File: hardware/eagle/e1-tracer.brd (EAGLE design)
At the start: 100 x 75 mm, 120 parts, among them IC1 MCP1703T-1202E/CB, IC2 W25Q80DVSNIG, IC3 TLV70233DBVR, IC4 ASEM1-12.000MHZ-LC-T, J1 PASSTHROUGH, M1 MENTOR_12701001, M2 MENTOR_12701001, SW1 TACTSW-TL3340, T1 BC847C, T2 BC847C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

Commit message: e1-tracer: start a last renumber (after inserting 4x 0R)
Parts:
- removed LOS0: LEDPLCC2-MIN-red, LED-PLCC2:PLCC2-MIN
- added LOS2: LEDPLCC2-MIN-red, LED-PLCC2:PLCC2-MIN
- C11: value 22u -> 100n; device rc-sysmocom:1206 -> rc-sysmocom:_0603
- C13: value 10n -> 22u; device rc-sysmocom:_0402 -> rc-sysmocom:1206
- C14: value 100n -> 10n; device rc-sysmocom:_0603 -> rc-sysmocom:_0402
- R11: value 68 -> 100k
- R12: value 10k -> 100k
- R14: value 10k -> 2.2k
- R15: value 10k -> 68
- R2, R3: value 33 -> DNP; device rc-sysmocom:_0402 -> rc-sysmocom:_0603
- R30, R31: value 3k 1% -> 10k
- R34, R35: value 120 -> 3k 1%
- R36, R37: value 330 -> 10k
- R38, R39: value 1k -> 120
- R4: value 1k5 -> DNP
- R40, R41: value DNP -> 330
- R42, R43: value DNP -> 1k
- R5: value 10k -> DNP
- R6, R7: value 100k -> 33; device rc-sysmocom:_0603 -> rc-sysmocom:_0402
- R9: value 2.2k -> 1k5
- moved R41 76.9 mm to (10.8, 23.2)
- moved R12 75.3 mm to (81.3, 10.8), turned to 270 degrees
- moved R40 70.3 mm to (15.2, 23.2)
- moved R33 67.2 mm to (66.3, 70.1), turned to 0 degrees
- moved R14 66.3 mm to (73.7, 18.1), turned to 90 degrees
- moved R13 61.2 mm to (80.0, 44.5), turned to 90 degrees
- moved R5 61.1 mm to (23.5, 32.7), turned to 180 degrees
- moved R46 61.0 mm to (73.1, 69.8), turned to 90 degrees
- moved R42 59.8 mm to (39.4, 20.4)
- moved R45 58.8 mm to (73.1, 68.2), turned to 90 degrees
- moved R44 58.4 mm to (75.0, 60.3), turned to 90 degrees
- moved R11 57.5 mm to (81.3, 14.0), turned to 270 degrees
- moved R4 54.8 mm to (25.1, 32.7)
- moved R3 54.1 mm to (23.5, 34.3), turned to 180 degrees
- moved R2 51.4 mm to (25.1, 34.3), turned to 180 degrees
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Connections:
- net CDONE: now also R14.2; no longer R9.2
- net GND: now also R11.1, R20.2, R29.2, R30.2, R31.2, R32.2, R34.1, R35.1, R45.2, R46.1; no longer R11.2, R12.2, R13.2, R14.2, R24.2, R30.1, R31.1, R41.2, R42.1, R6.1
- net IOB_34A_SPI_SCK: now also R10.1; no longer R8.1
- net IOB_35B_SPI_SS: now also R8.1; no longer R5.1
- net LOS0: now also R36.2; no longer R32.2
- net LOS1: now also R37.2; no longer R33.2
- net MCLK: now also R44.2; no longer R40.2
- net N$1: now also R35.2; no longer R31.2
- net N$10: now also R18.1; no longer R14.1
- net N$11: now also R19.1; no longer R15.1
- net N$12: now also R20.1; no longer R16.1
- net N$13: now also R21.1; no longer R17.1
- net N$14: now also R22.1; no longer R18.1
- net N$15: now also R27.1; no longer R23.1
- net N$16: now also R28.1; no longer R24.1
- net N$17: now also R24.1; no longer R20.1
- net N$18: now also R23.1; no longer R19.1
- net N$19: now also R29.1; no longer R25.1
- net N$2: now also R33.1; no longer R29.1
- net N$20: now also R30.1; no longer R26.1
- net N$21: now also R31.1; no longer R27.1
- net N$22: now also R32.1; no longer R28.1
- net N$25: now also R13.1; no longer R10.1
- net N$26: now also R36.1; no longer R32.1
- net N$27: now also LOS1.K, R40.1; no longer LOS0.K, R36.1
- net N$28: now also R40.2; no longer R36.2
- net N$29: now also R15.1; no longer R11.1
- net N$30: now also R42.1; no longer R38.1
- net N$31: now also R37.1; no longer R33.1
- net N$35: now also R45.1; no longer R41.1
- net N$37: now also LOS2.K, R41.1; no longer LOS1.K, R37.1
- net N$38: now also R46.2; no longer R42.2
- net N$39: now also R41.2; no longer R37.2
- net N$4: now also R34.2; no longer R30.2
- net N$41: now also R43.1; no longer R39.1
- net N$42: now also R42.2; no longer R38.2
- net N$45: now also R2.2, R3.1; no longer R45.2, R46.1
- net N$46: now also R3.2, R5.2; no longer R44.2, R46.2
- net N$5: now also R43.2; no longer R39.2
- net N$55: now also R11.2, R12.1; no longer R6.2, R7.1
- net N$6: now also R25.1; no longer R21.1
- net N$61: now also C14.1, R12.2; no longer C13.1, R7.2
- net N$63: now also R4.2, R5.1; no longer R43.2, R44.1
- net N$65: now also R2.1, R4.1; no longer R43.1, R45.1
- net N$7: now also R26.1; no longer R22.1
- net N$8: now also R16.1; no longer R12.1
- net N$9: now also R17.1; no longer R13.1
- net RRING: now also R38.1; no longer R34.1
- net RRING1: now also R39.1; no longer R35.1
- net RTIP: now also R38.2; no longer R34.2
- net RTIP1: now also R39.2; no longer R35.2
- net TCLK: now also R44.1; no longer R40.1
- net USB1_D_P: now also R9.2; no longer R4.2
- net USB_D_N: now also R6.1; no longer R2.1
- net USB_D_P: now also R7.1; no longer R3.1
- net USB_PU: now also R9.1; no longer R4.1
- net VBUS: now also C13.1; no longer C11.1
- net VCC_3V3: now also C11.1, LOS2.A, R13.2, R14.1, R24.2, R33.2; no longer C14.1, LOS0.A, R20.2, R29.2, R5.2, R9.1
- net _D_N: now also R6.2; no longer R2.2
- net _D_P: now also R7.2; no longer R3.2

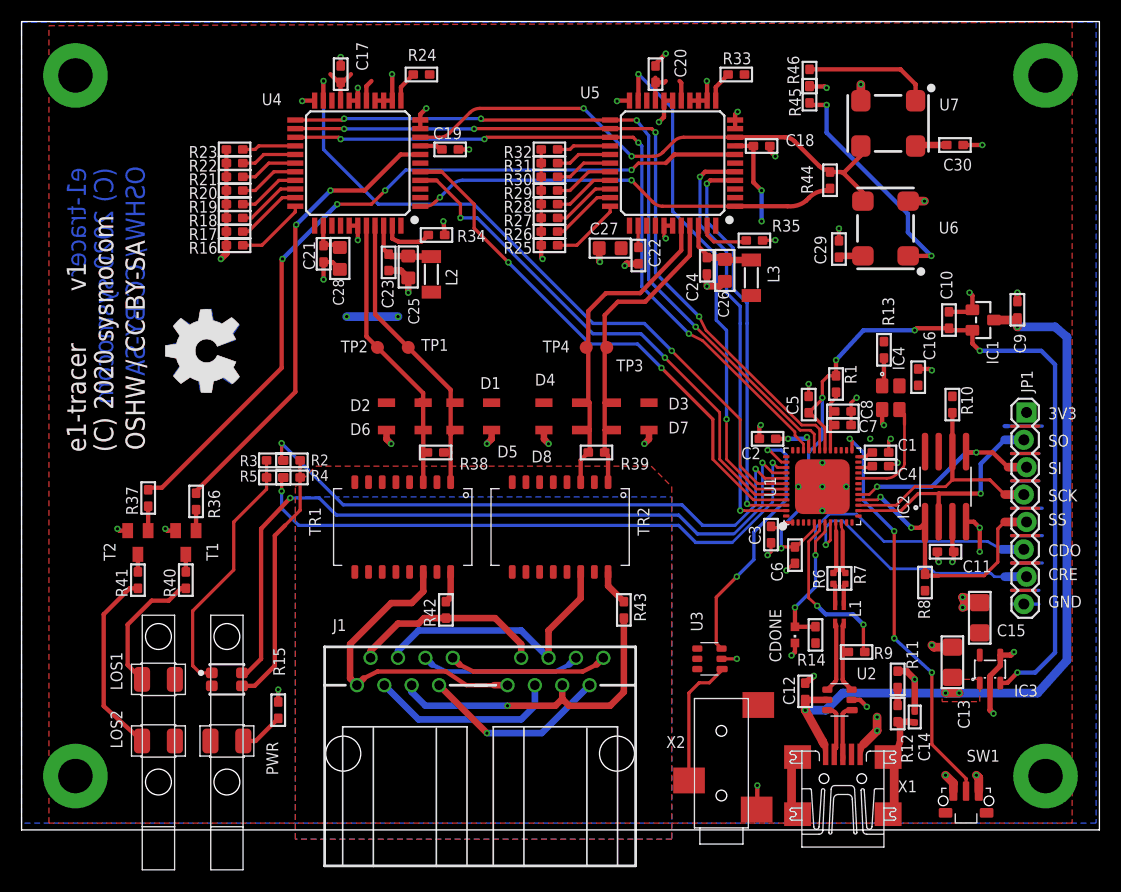
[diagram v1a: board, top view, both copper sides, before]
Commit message: e1-tracer: further shrink the GND and 3V3 copper inwards left and right
... and run a local DRC
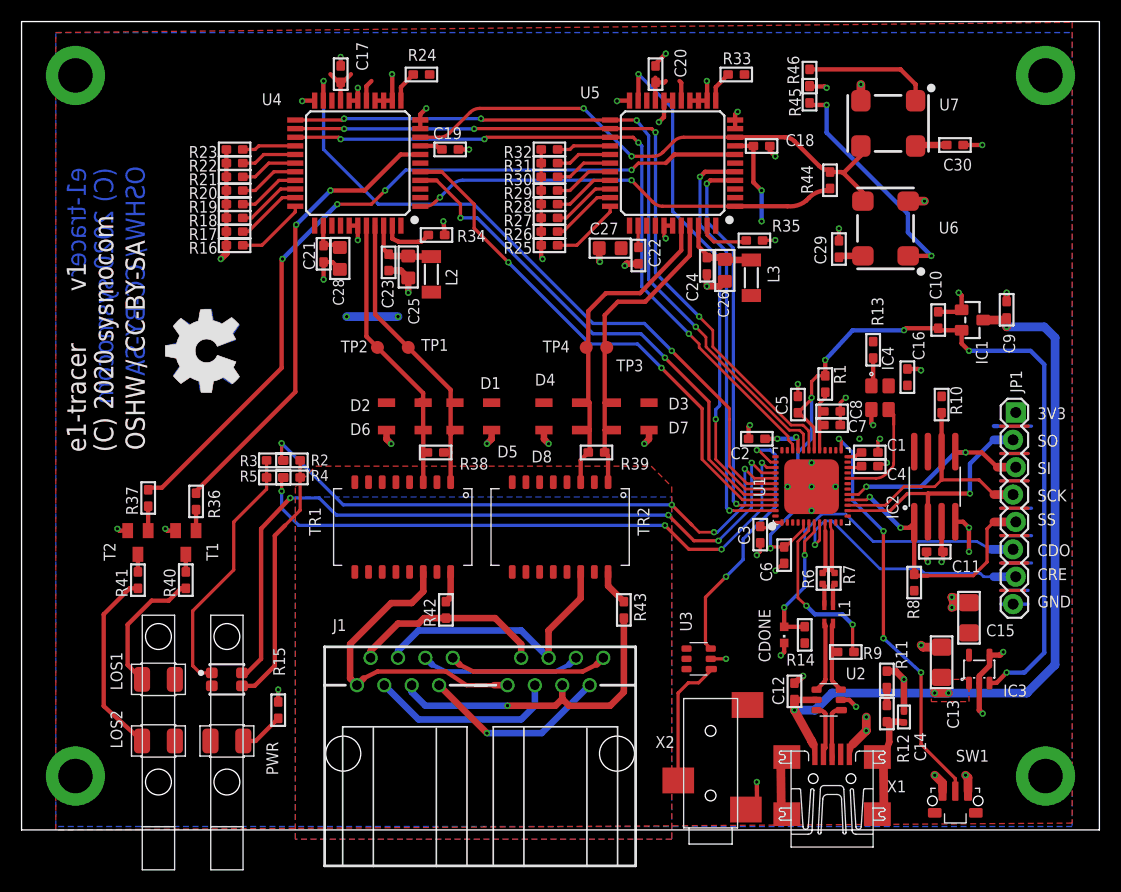
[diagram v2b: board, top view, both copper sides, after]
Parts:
- moved C1 1.00 mm to (78.7, 35.0)
- moved C10 1.00 mm to (85.0, 47.3)
- moved C11 1.00 mm to (84.7, 25.8)
- moved C12 1.00 mm to (71.7, 12.9)
- moved C13 1.00 mm to (85.4, 15.6)
- moved C14 1.00 mm to (81.9, 10.5)
- moved C15 1.00 mm to (87.9, 19.7)
- moved C16 1.00 mm to (82.2, 42.0)
- moved C2 1.00 mm to (68.2, 36.3)
- moved C3 1.00 mm to (68.5, 27.4)
- moved C4 1.00 mm to (78.7, 33.8)
- moved C5 1.00 mm to (72.0, 39.5)
- moved C6 1.00 mm to (70.8, 25.5)
- moved C7 1.00 mm to (75.2, 37.6)
- moved C8 1.00 mm to (75.2, 38.8)
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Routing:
- net GND: track 159.7 -> 160.6 mm, vias 73 -> 69
- net N$36: track 6.02 -> 6.82 mm
- net N$64: track 71.2 -> 70.8 mm, vias 2 -> 4
- net N$45: track 56.2 -> 55.9 mm, vias 2 -> 4
- net N$63: track 56.5 -> 56.4 mm, vias 2 -> 4

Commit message: e1-tracer: more eBOM atrributes + commit eBOM
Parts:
- R15: value 68 -> 330
